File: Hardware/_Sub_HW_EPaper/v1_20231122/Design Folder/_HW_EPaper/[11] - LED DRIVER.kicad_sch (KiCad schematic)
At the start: 4 parts

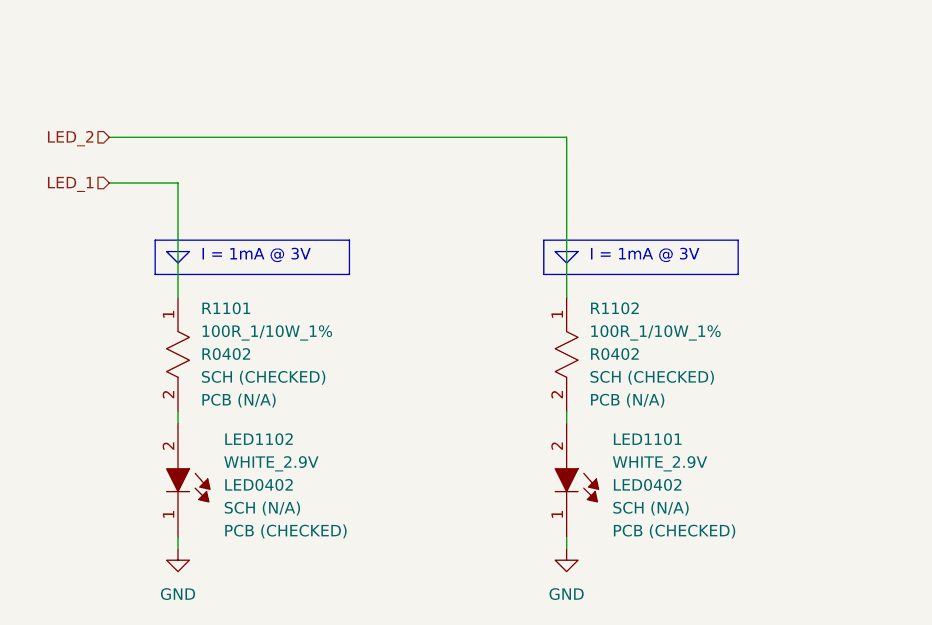
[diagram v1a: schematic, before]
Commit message: Working on epaper hardware
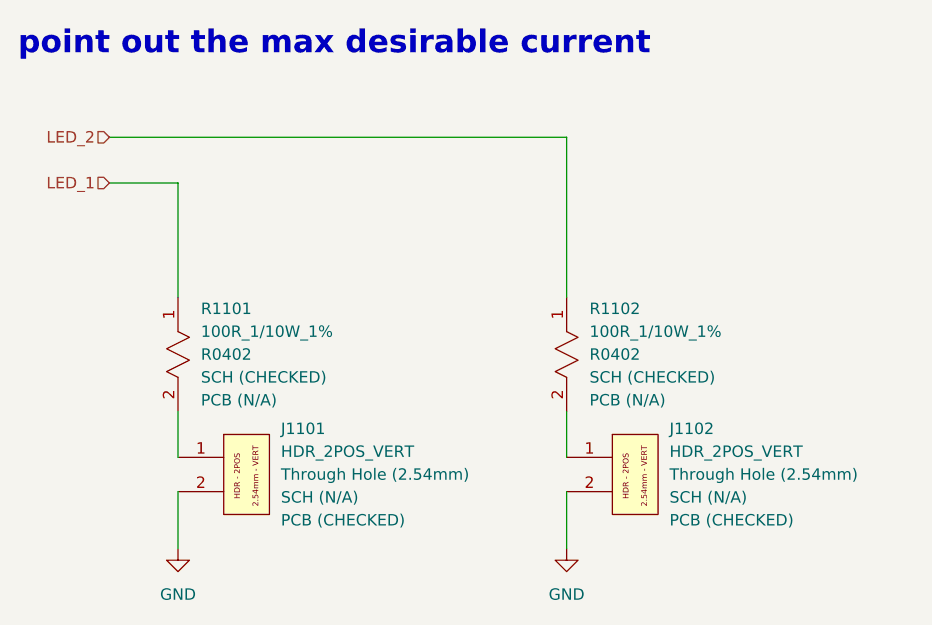
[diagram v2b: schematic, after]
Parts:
- removed LED1101, LED1102: WHITE_2.9V, LED_SMD:LED_0402_1005Metric, symbol _SCHLIB_Epaper:LED_WHITE_2.9V_LED0402
- added J1101, J1102: HDR_2POS_VERT, Connector_PinHeader_2.54mm:PinHeader_1x02_P2.54mm_Vertical, symbol _SCHLIB_Epaper:CONN_HEADER_2POS_1ROW_VERT_2.54mm
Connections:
- net GND: now also J1101.2, J1102.2
- net at R1102.2: now also J1102.1
- net at R1101.2: now also J1101.1
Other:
- note added: "point out the max desirable current"
- note removed: "I = 1mA @ 3V"

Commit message: Hardware is almost done
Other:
- note added: "DESIGN NOTE:"
- note added: "Imax ~= 5mA"
- note added: "You can connect any LED but the max current that can be sourced is 5mA"
- note removed: "point out the max desirable current"
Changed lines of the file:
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@@
     (comment 2 "CHECKED")
   )
+  (polyline (pts (xy 236.22 152.4) (xy 236.22 180.34))
+    (stroke (width 0) (type default))
+  )
   (wire (pts (xy 198.12 132.08) (xy 198.12 138.43))
+    (stroke (width 0) (type default))
+  )
+  (polyline (pts (xy 240.03 102.87) (xy 242.57 102.87))
+    (stroke (width 0) (type default))
+  )
+  (polyline (pts (xy 207.01 151.13) (xy 237.49 151.13))
+    (stroke (width 0) (type default))
+  )
+  (polyline (pts (xy 208.28 152.4) (xy 236.22 152.4))
+    (stroke (width 0) (type default))
+  )
+  (polyline (pts (xy 236.22 180.34) (xy 208.28 180.34))
     (stroke (width 0) (type default))
   )
@@
   )
   (wire (pts (xy 241.3 92.71) (xy 241.3 110.49))
+    (stroke (width 0) (type default))
+  )
+  (polyline (pts (xy 207.01 181.61) (xy 237.49 181.61))
     (stroke (width 0) (type default))
   )
@@
     (stroke (width 0) (type default))
   )
+  (polyline (pts (xy 196.85 102.87) (xy 199.39 102.87))
+    (stroke (width 0) (type default))
+  )
   (wire (pts (xy 198.12 97.79) (xy 198.12 110.49))
+    (stroke (width 0) (type default))
+  )
+  (polyline (pts (xy 241.3 104.14) (xy 242.57 102.87))
+    (stroke (width 0) (type default))
+  )
+  (polyline (pts (xy 198.12 104.14) (xy 199.39 102.87))
     (stroke (width 0) (type default))
   )
@@
     (stroke (width 0) (type default))
   )
-  (text "point out the max desirable current" (at 180.34 83.82 0)
-    (effects (font (size 2.54 2.54) bold) (justify left bottom))
+  (polyline (pts (xy 237.49 151.13) (xy 237.49 181.61))
+    (stroke (width 0) (type default))
+  )
+  (polyline (pts (xy 209.55 153.67) (xy 209.55 179.07))
+    (stroke (width 0) (type default))
+  )
+  (polyline (pts (xy 234.95 153.67) (xy 234.95 179.07))
+    (stroke (width 0) (type default))
+  )
+  (polyline (pts (xy 208.28 152.4) (xy 208.28 180.34))
+    (stroke (width 0) (type default))
+  )
+  (polyline (pts (xy 209.55 153.67) (xy 234.95 153.67))
+    (stroke (width 0) (type default))
+  )
+  (polyline (pts (xy 240.03 102.87) (xy 241.3 104.14))
+    (stroke (width 0) (type default))
+  )
+  (polyline (pts (xy 196.85 102.87) (xy 198.12 104.14))
+    (stroke (width 0) (type default))
+  )
+  (polyline (pts (xy 234.95 179.07) (xy 209.55 179.07))
+    (stroke (width 0) (type default))
+  )
+  (polyline (pts (xy 207.01 151.13) (xy 207.01 181.61))
+    (stroke (width 0) (type default))
+  )
+  (rectangle (start 195.58 101.6) (end 214.63 105.41)
+    (stroke (width 0) (type default))
+    (fill (type none))
+  )
+  (rectangle (start 238.76 101.6) (end 257.81 105.41)
+    (stroke (width 0) (type default))
+    (fill (type none))
+  )
+  (text "You can connect\nany LED but the\nmax current that\ncan be sourced\nis 5mA"
+    (at 213.36 170.18 0)
+    (effects (font (size 1.27 1.27)) (justify left bottom))
+  )
+  (text "DESIGN NOTE:" (at 210.82 158.75 0)
+    (effects (font (size 1.8 1.8) bold) (justify left bottom))
+  )
+  (text "Imax ~= 5mA" (at 243.84 104.14 0)
+    (effects (font (size 1.27 1.27)) (justify left bottom))
+  )
+  (text "Imax ~= 5mA" (at 200.66 104.14 0)
+    (effects (font (size 1.27 1.27)) (justify left bottom))
   )
   (hierarchical_label "LED_2" (shape input) (at 190.5 92.71 180) (fields_autoplaced)

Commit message: Updating file templates and structures...
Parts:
- J1101, J1102: Manufacturer (none) -> Adam Tech; Part Number PH1-02-UA -> (none); Part Number (Manufacturer) (none) -> PH1-02-UA; Part Number (Vendor) (none) -> 2057-PH1-02-UA-ND; Vendor (none) -> Digikey
- R1101, R1102: Manufacturer (none) -> KOA Speer Electronics, Inc.; Part Number RK73H1ETTP1000F -> (none); Part Number (Manufacturer) (none) -> RK73H1ETTP1000F; Part Number (Vendor) (none) -> 2019-RK73H1ETTP1000FTR-ND; Vendor (none) -> Digikey
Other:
- moved on the sheet: J1101, J1102, R1101, R1102

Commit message: Updating Hardware File structures
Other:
- note added: "You can connect any LED but the max current that can be sourced is 5mA for each output"
- note removed: "You can connect any LED but the max current that can be sourced is 5mA"
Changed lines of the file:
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@@
   (title_block
     (title "_HW_EPaper")
+    (date "2023-12-18")
     (rev "v1.0")
     (company "Mend0z0")
     (comment 1 "v1.0")
     (comment 2 "CHECKED")
+    (comment 3 "Siavash Taher Parvar")
+    (comment 4 "_BOM_EPaper.csv")
+    (comment 5 "_HW_EPaper.kicad_pcb")
+    (comment 6 "_GBR_EPaper.zip")
+    (comment 7 "_ASM_EPaper.html")
+    (comment 8 "N/A")
+    (comment 9 "First Release")
   )
   (polyline (pts (xy 274.32 207.01) (xy 274.32 234.95))
@@
     (fill (type none))
   )
-  (text "You can connect\nany LED but the\nmax current that\ncan be sourced\nis 5mA"
-    (at 251.46 224.79 0)
+  (text "You can connect\nany LED but the\nmax current that\ncan be sourced\nis 5mA for each output"
+    (at 248.92 224.79 0)
     (effects (font (size 1.27 1.27)) (justify left bottom))
   )
